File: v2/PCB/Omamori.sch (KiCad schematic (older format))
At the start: 12 parts, among them U1 BQ25504, U2 ATtiny13A-SSU

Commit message: Modified PCB and updated Software.
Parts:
- added D10, D11, D12, D13, D14, D15, D16, D17, D18, D19, D20, D21: BPW34, own_footprints:Osram_DIL2_4.3x4.65mm_P5.08mm, symbol Sensor_Optical:BPW34
- CSuper1: footprint Capacitor_THT:C_Rect_L7.2mm_W2.5mm_P5.00mm_FKS2_FKP2_MKS2_MKP2 -> Capacitor_THT:C_Radial_D10.0mm_H12.5mm_P5.00mm
- D1, D2, D3, D4, D5, D6, D7, D8: footprint OptoDevice:Osram_DIL2_4.3x4.65mm_P5.08mm -> own_footprints:Osram_DIL2_4.3x4.65mm_P5.08mm
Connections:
- wire segments 16 -> 54

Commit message: Updated version 2 PCB.
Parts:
- removed D1, D10, D11, D12, D13, D14, D15, D16, D17, D18, D19, D2, D20, D21, D3, D4, D5, D6, D7, D8: BPW34, own_footprints:Osram_DIL2_4.3x4.65mm_P5.08mm, symbol Sensor_Optical:BPW34
- added C_filter1: 0.1uF, Capacitor_SMD:C_0603_1608Metric_Pad1.05x0.95mm_HandSolder, symbol Device:C
- added C_hvr1: 4.7uF, Capacitor_SMD:C_0603_1608Metric_Pad1.05x0.95mm_HandSolder, symbol Device:C
- added C_led1: 100nF, Capacitor_SMD:C_0603_1608Metric_Pad1.05x0.95mm_HandSolder, symbol Device:C
- added C_post_boost1, C_pre_boost1: 10uF, Capacitor_SMD:C_0603_1608Metric_Pad1.05x0.95mm_HandSolder, symbol Device:C
- added C_ref1: 0.01uF, Capacitor_SMD:C_0603_1608Metric_Pad1.05x0.95mm_HandSolder, symbol Device:C
- added J1: Conn_01x04_Female, Connector_PinHeader_1.27mm:PinHeader_1x04_P1.27mm_Horizontal, symbol Connector:Conn_01x04_Female
- added L_boost1: 4.7uH, Inductor_SMD:L_Wuerth_MAPI-3015, symbol Device:L
- added L_bst1: 22uH, Inductor_SMD:L_Wuerth_MAPI-3015, symbol Device:L
- added R1: 1M, Resistor_SMD:R_0603_1608Metric_Pad1.05x0.95mm_HandSolder, symbol Device:R
- added R_data1: 500, Resistor_SMD:R_0603_1608Metric_Pad1.05x0.95mm_HandSolder, symbol Device:R
- added R_oc1: 3.9M, Resistor_SMD:R_0603_1608Metric_Pad1.05x0.95mm_HandSolder, symbol Device:R
- added R_oc2, R_ok3, R_ov1: 6.2M, Resistor_SMD:R_0603_1608Metric_Pad1.05x0.95mm_HandSolder, symbol Device:R
- added R_ok1: 2.4M, Resistor_SMD:R_0603_1608Metric_Pad1.05x0.95mm_HandSolder, symbol Device:R
- added R_ok2, R_uv1: 1.6M, Resistor_SMD:R_0603_1608Metric_Pad1.05x0.95mm_HandSolder, symbol Device:R
- added R_ov2: 3.3M, Resistor_SMD:R_0603_1608Metric_Pad1.05x0.95mm_HandSolder, symbol Device:R
- added R_uv2: 8.2M, Resistor_SMD:R_0603_1608Metric_Pad1.05x0.95mm_HandSolder, symbol Device:R
- added Sol_1, Sol_2: KXOB25-05X3F, own_footprints:KXOB25-05X3F, symbol own_symbols:KXOB25-05X3F
- added U2: TPS61222DCK, Package_TO_SOT_SMD:Texas_R-PDSO-G6, symbol Regulator_Switching:TPS61222DCK
- C_super1: renamed from CSuper1; value C -> 640mF; footprint Capacitor_THT:C_Radial_D10.0mm_H12.5mm_P5.00mm -> own_footprints:Supercap
- renumbered D9 to D1, U2 to U3
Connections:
- wire segments 54 -> 65
- no-connect marks 1 -> 2
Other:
- moved on the sheet: D1, U3

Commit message: Updated PCB layout and added gerber and pictures.
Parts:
- removed R1: 1M, Resistor_SMD:R_0603_1608Metric_Pad1.05x0.95mm_HandSolder, symbol Device:R
- added D2: DIODE, Diode_SMD:D_SOD-323_HandSoldering, symbol pspice:DIODE
- Sol_1, Sol_2: symbol own_symbols:KXOB25-05X3F -> Omamori-rescue:KXOB25-05X3F-own_symbols
- U3: value ATtiny13A-SSU -> ATtiny85
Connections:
- net labels added: Data_LED, Din_LED, Rx, Tx, Vbat_ok, Vcc_ATTiny, Vcc_LED, Vr_div, Vsolar, Vsolar_measure, Vstor
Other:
- moved on the sheet: C_filter1
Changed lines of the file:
@@
 P 8300 3600
 F 0 "U3" V 7725 3600 50  0000 C CNN
-F 1 "ATtiny13A-SSU" V 7634 3600 50  0000 C CNN
+F 1 "ATtiny85" V 7634 3600 50  0000 C CNN
 F 2 "Package_SO:SOIC-8_3.9x4.9mm_P1.27mm" H 8300 3600 50  0001 C CIN
 F 3 "http://ww1.microchip.com/downloads/en/DeviceDoc/doc8126.pdf" H 8300 3600 50  0001 C CNN
@@
 $EndComp
 $Comp
-L own_symbols:KXOB25-05X3F Sol_1
+L Omamori-rescue:KXOB25-05X3F-own_symbols Sol_1
 U 1 1 609C9A98
 P 2550 2500
@@
 $EndComp
 $Comp
-L own_symbols:KXOB25-05X3F Sol_2
+L Omamori-rescue:KXOB25-05X3F-own_symbols Sol_2
 U 1 1 609C8E61
 P 2550 3300
@@
 	1    0    0    -1
 $EndComp
-$Comp
-L Device:C C_filter1
-U 1 1 609F4440
-P 5800 2600
-F 0 "C_filter1" H 5915 2646 50  0000 L CNN
-F 1 "0.1uF" H 5915 2555 50  0000 L CNN
-F 2 "Capacitor_SMD:C_0603_1608Metric_Pad1.05x0.95mm_HandSolder" H 5838 2450 50  0001 C CNN
-F 3 "~" H 5800 2600 50  0001 C CNN
-	1    5800 2600
-	1    0    0    -1
-$EndComp
-$Comp
-L power:GND #PWR014
-U 1 1 609F4F40
-P 5800 2750
-F 0 "#PWR014" H 5800 2500 50  0001 C CNN
-F 1 "GND" H 5805 2577 50  0000 C CNN
-F 2 "" H 5800 2750 50  0001 C CNN
-F 3 "" H 5800 2750 50  0001 C CNN
-	1    5800 2750
-	1    0    0    -1
-$EndComp
-Wire Wire Line
-	5800 2450 5200 2450
-Connection ~ 5200 2450
 $Comp
 L power:GND #PWR08
@@
 	6950 1150 6950 3600
 Wire Wire Line
-	4150 1750 4150 2050
-Wire Wire Line
 	5650 3700 5950 3700
 $Comp
@@
 $EndComp
 Wire Wire Line
-	4150 1750 7250 1750
-Wire Wire Line
-	8000 1750 8000 3000
-Wire Wire Line
 	8000 1150 6950 1150
 NoConn ~ 8500 3000
-$Comp
-L Device:R R1
-U 1 1 60AE19CB
-P 7400 1750
-F 0 "R1" V 7193 1750 50  0000 C CNN
-F 1 "1M" V 7284 1750 50  0000 C CNN
-F 2 "Resistor_SMD:R_0603_1608Metric_Pad1.05x0.95mm_HandSolder" V 7330 1750 50  0001 C CNN
-F 3 "~" H 7400 1750 50  0001 C CNN
-	1    7400 1750
-	0    1    1    0
-$EndComp
-Wire Wire Line
-	7550 1750 8000 1750
 Wire Wire Line
 	8100 1150 8100 2350
@@
 Wire Wire Line
 	8200 2350 8200 3000
-Wire Wire Line
-	8100 3000 8100 2500
-Wire Wire Line
-	8100 2500 8300 2500
-Wire Wire Line
-	8300 2500 8300 2200
-Wire Wire Line
-	8300 2200 8200 2200
-Wire Wire Line
-	8200 2200 8200 1150
 Wire Wire Line
 	6950 3600 7700 3600
@@
 $EndComp
 Wire Wire Line
-	5150 3700 5650 3700
+	5150 3700 5300 3700
+Wire Wire Line
+	8200 1150 8200 2300
+Wire Wire Line
+	8200 2300 8300 2300
+Wire Wire Line
+	8300 2300 8300 2650
+Wire Wire Line
+	8300 2650 8100 2650
+Wire Wire Line
+	8100 2650 8100 3000
+$Comp
+L pspice:DIODE D2
+U 1 1 60AAB4F1
+P 6100 1800
+F 0 "D2" H 6100 1535 50  0000 C CNN
+F 1 "DIODE" H 6100 1626 50  0000 C CNN
+F 2 "Diode_SMD:D_SOD-323_HandSoldering" H 6100 1800 50  0001 C CNN
+F 3 "~" H 6100 1800 50  0001 C CNN
+	1    6100 1800
+	-1   0    0    1
+$EndComp
+Wire Wire Line
+	8000 1800 6300 1800
+Text Label 2850 2050 0    50   ~ 0
+Vsolar
+Wire Wire Line
+	5900 1800 3300 1800
+Wire Wire Line
+	3300 1800 3300 2050
+Wire Wire Line
+	8000 1800 8000 3000
+Text Label 7250 3600 0    50   ~ 0
+Vcc_ATTiny
+Text Label 5350 3100 0    50   ~ 0
+Vbat_ok
+Text Label 5300 3700 0    50   ~ 0
+Vstor
+Text Label 3450 3200 0    50   ~ 0
+Vr_div
+$Comp
+L power:GND #PWR014
+U 1 1 609F4F40
+P 5300 4000
+F 0 "#PWR014" H 5300 3750 50  0001 C CNN
+F 1 "GND" H 5305 3827 50  0000 C CNN
+F 2 "" H 5300 4000 50  0001 C CNN
+F 3 "" H 5300 4000 50  0001 C CNN
+	1    5300 4000
+	1    0    0    -1
+$EndComp
+$Comp
+L Device:C C_filter1
+U 1 1 609F4440
+P 5300 3850
+F 0 "C_filter1" H 5415 3896 50  0000 L CNN
+F 1 "0.1uF" H 5415 3805 50  0000 L CNN
+F 2 "Capacitor_SMD:C_0603_1608Metric_Pad1.05x0.95mm_HandSolder" H 5338 3700 50  0001 C CNN
+F 3 "~" H 5300 3850 50  0001 C CNN
+	1    5300 3850
+	1    0    0    -1
+$EndComp
+Connection ~ 5300 3700
+Wire Wire Line
+	5300 3700 5650 3700
+Text Label 7300 1800 0    50   ~ 0
+Vsolar_measure
+Text Label 8200 1550 0    50   ~ 0
+Tx
+Text Label 8100 1550 0    50   ~ 0
+Rx
+Text Label 9450 2800 0    50   ~ 0
+Vcc_LED
+Text Label 8550 2900 0    50   ~ 0
+Data_LED
+Text Label 9150 3100 0    50   ~ 0
+Din_LED
 $EndSCHEMATC

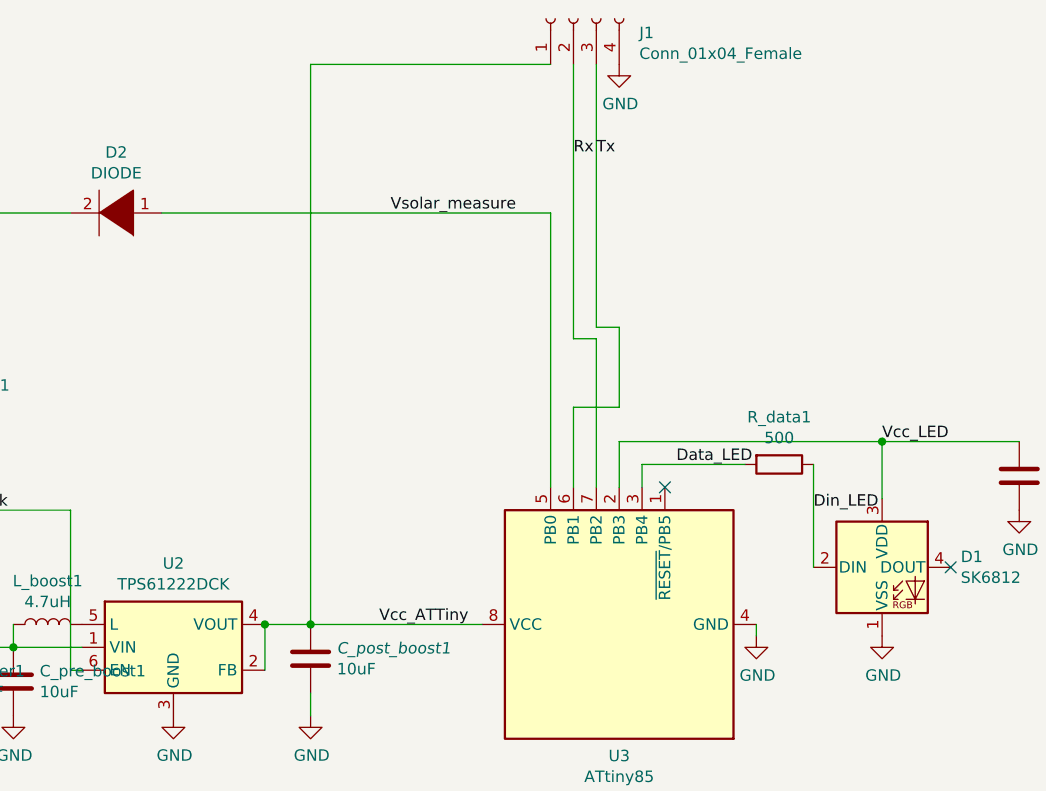
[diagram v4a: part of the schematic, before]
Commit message: Added reset button and changed a few wires.
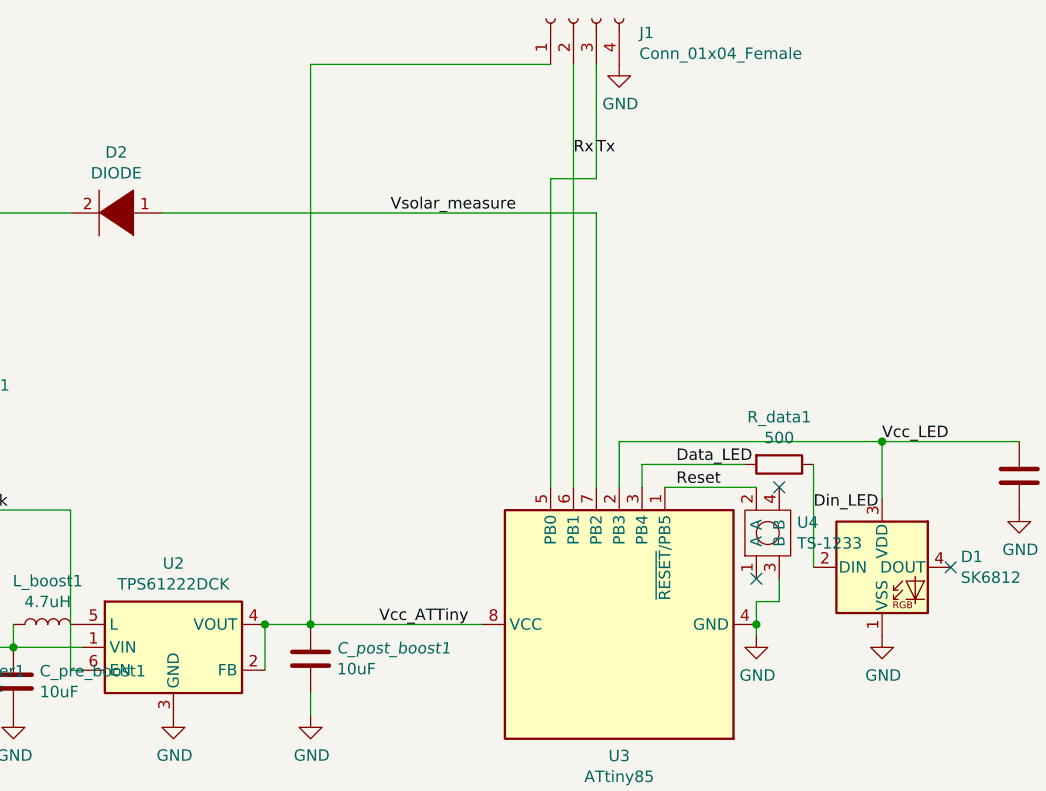
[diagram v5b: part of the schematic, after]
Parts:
- added U4: TS-1233, own_footprints:TS-1233, symbol own_symbols:TS-1233
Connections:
- net GND: now also U4.3 (B)
- net Rx: now also U3.6 (PB1); no longer U3.7 (PB2)
- net Tx: now also U3.5 (PB0); no longer U3.6 (PB1)
- net Vsolar_measure: now also U3.7 (PB2); no longer U3.5 (PB0)
- net Reset: now reaches U3.1 (~RESET~/PB5)
- net Reset: now also U4.2 (A)
- no-connect marks 2 -> 3
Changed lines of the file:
@@
 Wire Wire Line
 	8000 1150 6950 1150
-NoConn ~ 8500 3000
-Wire Wire Line
-	8100 1150 8100 2350
-Wire Wire Line
-	8100 2350 8200 2350
-Wire Wire Line
-	8200 2350 8200 3000
 Wire Wire Line
 	6950 3600 7700 3600
@@
 Wire Wire Line
 	5150 3700 5300 3700
-Wire Wire Line
-	8200 1150 8200 2300
-Wire Wire Line
-	8200 2300 8300 2300
-Wire Wire Line
-	8300 2300 8300 2650
-Wire Wire Line
-	8300 2650 8100 2650
-Wire Wire Line
-	8100 2650 8100 3000
 $Comp
 L pspice:DIODE D2
@@
 	-1   0    0    1
 $EndComp
-Wire Wire Line
-	8000 1800 6300 1800
 Text Label 2850 2050 0    50   ~ 0
 Vsolar
@@
 Wire Wire Line
 	3300 1800 3300 2050
-Wire Wire Line
-	8000 1800 8000 3000
 Text Label 7250 3600 0    50   ~ 0
 Vcc_ATTiny
@@
 	0    -1   -1   0
 $EndComp
+Wire Wire Line
+	8200 1800 8200 3000
+Wire Wire Line
+	6300 1800 8200 1800
+Wire Wire Line
+	8100 3000 8100 1150
+Wire Wire Line
+	8200 1150 8200 1650
+Wire Wire Line
+	8200 1650 8000 1650
+Wire Wire Line
+	8000 1650 8000 3000
+Wire Wire Line
+	8900 3500 8900 3600
+Connection ~ 8900 3600
+Text Label 8550 3000 0    50   ~ 0
+Reset
+Wire Wire Line
+	9000 3400 9000 3500
+Wire Wire Line
+	8500 3000 8900 3000
+$Comp
+L own_symbols:TS-1233 U4
+U 1 1 60ACC29B
+P 8950 3200
+F 0 "U4" V 8996 3072 50  0000 R CNN
+F 1 "TS-1233" V 8905 3072 50  0000 R CNN
+F 2 "own_footprints:TS-1233" H 8950 3050 50  0001 C CNN
+F 3 "" H 8950 3050 50  0001 C CNN
+	1    8950 3200
+	0    -1   -1   0
+$EndComp
+NoConn ~ 8900 3400
+Wire Wire Line
+	8900 3500 9000 3500
+NoConn ~ 9000 3000
 $EndSCHEMATC

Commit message: Updated program and modified PCB Layout to measure V_supercap.
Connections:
- net Vsolar: no longer D2.2 (A)
- net at C_super1.1, U1.14 (VBAT): now also D2.2 (A)
- net Vsolar_measure renamed Vmeasure
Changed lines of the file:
@@
 Text Label 2850 2050 0    50   ~ 0
 Vsolar
-Wire Wire Line
-	5900 1800 3300 1800
-Wire Wire Line
-	3300 1800 3300 2050
 Text Label 7250 3600 0    50   ~ 0
 Vcc_ATTiny
@@
 	5300 3700 5650 3700
 Text Label 7300 1800 0    50   ~ 0
-Vsolar_measure
+Vmeasure
 Text Label 8200 1550 0    50   ~ 0
 Tx
@@
 	8900 3500 9000 3500
 NoConn ~ 9000 3000
+Wire Wire Line
+	5900 1800 5200 1800
+Wire Wire Line
+	5200 1800 5200 2450
+Connection ~ 5200 2450
 $EndSCHEMATC

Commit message: Beyond last second changes to the PCB design and gerber files.
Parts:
- added R_oc1: 6.2M, Resistor_SMD:R_0603_1608Metric_Pad0.98x0.95mm_HandSolder, symbol Device:R
- R_oc1_10: renamed from R_oc1; value 3.9M -> 10M
- R_oc2: value 6.2M -> 3.9M
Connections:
- net at R_oc2.1, U1.3 (VOC_SAMP): now also R_oc1.2; no longer R_oc1_10.2
- new net: R_oc1.1, R_oc1_10.2
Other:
- moved on the sheet: R_oc2
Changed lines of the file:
@@
-$EndComp
-$Comp
-L Battery_Management:BQ25504 U1
-U 1 1 6049F0BD
-P 4550 3400
-F 0 "U1" H 5194 3446 50  0000 L CNN
-F 1 "BQ25504" H 5194 3355 50  0000 L CNN
-F 2 "footprints:VQFN-16-1EP_3x3mm_P0.5mm_EP1.8x1.8mm" H 4550 3400 50  0001 C CNN
-F 3 "http://www.ti.com/lit/ds/symlink/bq25504.pdf" H 4250 4200 50  0001 C CNN
-	1    4550 3400
-	1    0    0    -1
 $EndComp
 $Comp
@@
 Connection ~ 4150 2050
 $Comp
-L Device:R R_oc1
+L Device:R R_oc1_10
 U 1 1 609D50F7
 P 3750 2300
-F 0 "R_oc1" H 3820 2346 50  0000 L CNN
-F 1 "3.9M" H 3820 2255 50  0000 L CNN
+F 0 "R_oc1_10" H 3820 2346 50  0000 L CNN
+F 1 "10M" H 3820 2255 50  0000 L CNN
 F 2 "Resistor_SMD:R_0603_1608Metric_Pad1.05x0.95mm_HandSolder" V 3680 2300 50  0001 C CNN
 F 3 "~" H 3750 2300 50  0001 C CNN
@@
 L Device:R R_oc2
 U 1 1 609D577E
-P 3750 2600
-F 0 "R_oc2" H 3820 2646 50  0000 L CNN
-F 1 "6.2M" H 3820 2555 50  0000 L CNN
-F 2 "Resistor_SMD:R_0603_1608Metric_Pad1.05x0.95mm_HandSolder" V 3680 2600 50  0001 C CNN
-F 3 "~" H 3750 2600 50  0001 C CNN
-	1    3750 2600
-	1    0    0    -1
+P 3600 2950
+F 0 "R_oc2" H 3670 2996 50  0000 L CNN
+F 1 "3.9M" H 3670 2905 50  0000 L CNN
+F 2 "Resistor_SMD:R_0603_1608Metric_Pad1.05x0.95mm_HandSolder" V 3530 2950 50  0001 C CNN
+F 3 "~" H 3600 2950 50  0001 C CNN
+	1    3600 2950
+	0    1    1    0
 $EndComp
 Wire Wire Line
@@
 Wire Wire Line
 	3750 2050 4150 2050
-Wire Wire Line
-	3750 2450 3950 2450
-Wire Wire Line
-	3950 2450 3950 3100
-Connection ~ 3750 2450
 $Comp
 L power:GND #PWR06
 U 1 1 609DECA8
-P 3750 2750
-F 0 "#PWR06" H 3750 2500 50  0001 C CNN
-F 1 "GND" H 3755 2577 50  0000 C CNN
-F 2 "" H 3750 2750 50  0001 C CNN
-F 3 "" H 3750 2750 50  0001 C CNN
-	1    3750 2750
-	1    0    0    -1
+P 3450 2950
+F 0 "#PWR06" H 3450 2700 50  0001 C CNN
+F 1 "GND" H 3455 2777 50  0000 C CNN
+F 2 "" H 3450 2950 50  0001 C CNN
+F 3 "" H 3450 2950 50  0001 C CNN
+	1    3450 2950
+	0    1    1    0
 $EndComp
 Wire Wire Line
@@
 	5200 1800 5200 2450
 Connection ~ 5200 2450
+$Comp
+L Battery_Management:BQ25504 U1
+U 1 1 6049F0BD
+P 4550 3400
+F 0 "U1" H 5194 3446 50  0000 L CNN
+F 1 "BQ25504" H 5194 3355 50  0000 L CNN
+F 2 "footprints:VQFN-16-1EP_3x3mm_P0.5mm_EP1.8x1.8mm" H 4550 3400 50  0001 C CNN
+F 3 "http://www.ti.com/lit/ds/symlink/bq25504.pdf" H 4250 4200 50  0001 C CNN
+	1    4550 3400
+	1    0    0    -1
+$EndComp
+Wire Wire Line
+	3950 3100 3950 2950
+Wire Wire Line
+	3950 2950 3750 2950
+$Comp
+L Device:R R_oc1
+U 1 1 60AEA81A
+P 3750 2700
+F 0 "R_oc1" H 3820 2746 50  0000 L CNN
+F 1 "6.2M" H 3820 2655 50  0000 L CNN
+F 2 "Resistor_SMD:R_0603_1608Metric_Pad0.98x0.95mm_HandSolder" V 3680 2700 50  0001 C CNN
+F 3 "~" H 3750 2700 50  0001 C CNN
+	1    3750 2700
+	1    0    0    -1
+$EndComp
+Wire Wire Line
+	3750 2850 3750 2950
+Connection ~ 3750 2950
+Wire Wire Line
+	3750 2550 3750 2450
 $EndSCHEMATC

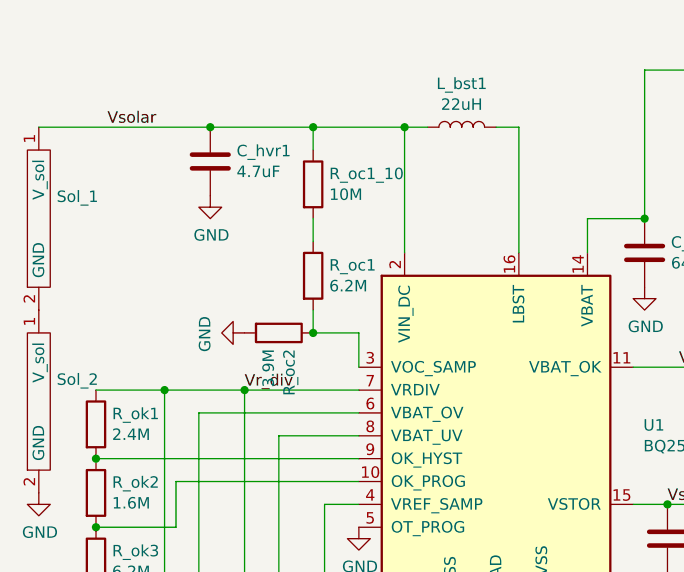
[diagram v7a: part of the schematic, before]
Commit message: Changes made to Roc1 and Roc2.
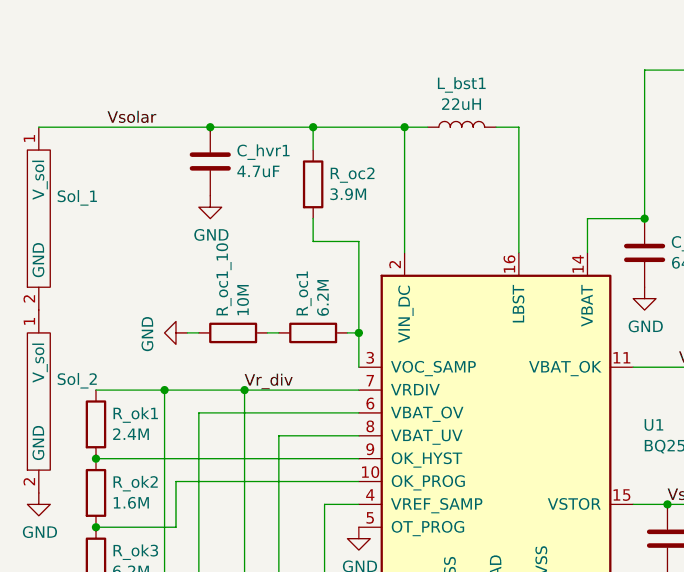
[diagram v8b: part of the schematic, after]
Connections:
- net GND: now also R_oc1_10.1; no longer R_oc2.2
- net Vsolar: now also R_oc2.1; no longer R_oc1_10.1
- net at R_oc1.2, U1.3 (VOC_SAMP): now also R_oc2.2; no longer R_oc2.1
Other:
- moved on the sheet: R_oc1, R_oc1_10, R_oc2
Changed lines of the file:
@@
 L Device:R R_oc1_10
 U 1 1 609D50F7
+P 3400 2950
+F 0 "R_oc1_10" H 3470 2996 50  0000 L CNN
+F 1 "10M" H 3470 2905 50  0000 L CNN
+F 2 "Resistor_SMD:R_0603_1608Metric_Pad1.05x0.95mm_HandSolder" V 3330 2950 50  0001 C CNN
+F 3 "~" H 3400 2950 50  0001 C CNN
+	1    3400 2950
+	0    -1   -1   0
+$EndComp
+$Comp
+L Device:R R_oc2
+U 1 1 609D577E
 P 3750 2300
-F 0 "R_oc1_10" H 3820 2346 50  0000 L CNN
-F 1 "10M" H 3820 2255 50  0000 L CNN
+F 0 "R_oc2" H 3820 2346 50  0000 L CNN
+F 1 "3.9M" H 3820 2255 50  0000 L CNN
 F 2 "Resistor_SMD:R_0603_1608Metric_Pad1.05x0.95mm_HandSolder" V 3680 2300 50  0001 C CNN
 F 3 "~" H 3750 2300 50  0001 C CNN
@@
 	1    0    0    -1
 $EndComp
-$Comp
-L Device:R R_oc2
-U 1 1 609D577E
-P 3600 2950
-F 0 "R_oc2" H 3670 2996 50  0000 L CNN
-F 1 "3.9M" H 3670 2905 50  0000 L CNN
-F 2 "Resistor_SMD:R_0603_1608Metric_Pad1.05x0.95mm_HandSolder" V 3530 2950 50  0001 C CNN
-F 3 "~" H 3600 2950 50  0001 C CNN
-	1    3600 2950
-	0    1    1    0
-$EndComp
 Wire Wire Line
 	3750 2150 3750 2050
@@
 L power:GND #PWR06
 U 1 1 609DECA8
-P 3450 2950
-F 0 "#PWR06" H 3450 2700 50  0001 C CNN
-F 1 "GND" H 3455 2777 50  0000 C CNN
-F 2 "" H 3450 2950 50  0001 C CNN
-F 3 "" H 3450 2950 50  0001 C CNN
-	1    3450 2950
+P 3200 2950
+F 0 "#PWR06" H 3200 2700 50  0001 C CNN
+F 1 "GND" H 3205 2777 50  0000 C CNN
+F 2 "" H 3200 2950 50  0001 C CNN
+F 3 "" H 3200 2950 50  0001 C CNN
+	1    3200 2950
 	0    1    1    0
 $EndComp
@@
 	1    0    0    -1
 $EndComp
-Wire Wire Line
-	3950 3100 3950 2950
-Wire Wire Line
-	3950 2950 3750 2950
 $Comp
 L Device:R R_oc1
 U 1 1 60AEA81A
-P 3750 2700
-F 0 "R_oc1" H 3820 2746 50  0000 L CNN
-F 1 "6.2M" H 3820 2655 50  0000 L CNN
-F 2 "Resistor_SMD:R_0603_1608Metric_Pad0.98x0.95mm_HandSolder" V 3680 2700 50  0001 C CNN
-F 3 "~" H 3750 2700 50  0001 C CNN
-	1    3750 2700
-	1    0    0    -1
-$EndComp
-Wire Wire Line
-	3750 2850 3750 2950
-Connection ~ 3750 2950
+P 3750 2950
+F 0 "R_oc1" H 3820 2996 50  0000 L CNN
+F 1 "6.2M" H 3820 2905 50  0000 L CNN
+F 2 "Resistor_SMD:R_0603_1608Metric_Pad0.98x0.95mm_HandSolder" V 3680 2950 50  0001 C CNN
+F 3 "~" H 3750 2950 50  0001 C CNN
+	1    3750 2950
+	0    -1   -1   0
+$EndComp
 Wire Wire Line
 	3750 2550 3750 2450
+Wire Wire Line
+	3750 2550 3950 2550
+Wire Wire Line
+	3950 2550 3950 2950
+Wire Wire Line
+	3900 2950 3950 2950
+Connection ~ 3950 2950
+Wire Wire Line
+	3950 2950 3950 3100
+Wire Wire Line
+	3600 2950 3550 2950
+Wire Wire Line
+	3250 2950 3200 2950
 $EndSCHEMATC
